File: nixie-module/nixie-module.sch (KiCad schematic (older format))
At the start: 4 parts, among them P1 CONN_02X05, U1 74141

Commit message: Kondensator przy zasilaniu ukladu 74141
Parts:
- added C1: 100n, symbol C
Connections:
- net GND: now also C1.2
- net VCC: now also C1.1
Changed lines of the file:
@@
 Connection ~ 2350 3450
 Connection ~ 2600 4050
+$Comp
+L C C1
+U 1 1 5832D96B
+P 2700 2800
+F 0 "C1" H 2725 2900 50  0000 L CNN
+F 1 "100n" H 2725 2700 50  0000 L CNN
+F 2 "" H 2738 2650 50  0000 C CNN
+F 3 "" H 2700 2800 50  0000 C CNN
+	1    2700 2800
+	1    0    0    -1
+$EndComp
+$Comp
+L GND #PWR?
+U 1 1 5832DA1C
+P 2700 3050
+F 0 "#PWR?" H 2700 2800 50  0001 C CNN
+F 1 "GND" H 2700 2900 50  0000 C CNN
+F 2 "" H 2700 3050 50  0000 C CNN
+F 3 "" H 2700 3050 50  0000 C CNN
+	1    2700 3050
+	1    0    0    -1
+$EndComp
+Wire Wire Line
+	2700 2650 2700 2550
+Wire Wire Line
+	2700 2550 2350 2550
+Connection ~ 2350 2550
+Wire Wire Line
+	2700 2950 2700 3050
 $EndSCHEMATC

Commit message: Przypisanie elementow (poza lampa) do obudow
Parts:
- C1: footprint (none) -> Capacitors_SMD:C_0805_HandSoldering
- P1: footprint (none) -> Pin_Headers:Pin_Header_Angled_2x05
- R1: footprint (none) -> Resistors_SMD:R_1812_HandSoldering
- U1: footprint (none) -> Housings_DIP:DIP-16_W7.62mm_LongPads
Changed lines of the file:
@@
 F 0 "U1" H 4950 3700 50  0000 C CNN
 F 1 "74141" H 5250 3100 50  0000 C CNN
-F 2 "" H 4950 3700 60  0001 C CNN
+F 2 "Housings_DIP:DIP-16_W7.62mm_LongPads" H 4950 3700 60  0001 C CNN
 F 3 "" H 4950 3700 60  0001 C CNN
 	1    4950 3700
@@
 F 0 "R1" V 7080 2950 50  0000 C CNN
 F 1 "100k" V 7000 2950 50  0000 C CNN
-F 2 "" V 6930 2950 50  0000 C CNN
+F 2 "Resistors_SMD:R_1812_HandSoldering" V 6930 2950 50  0001 C CNN
 F 3 "" H 7000 2950 50  0000 C CNN
 	1    7000 2950
@@
 F 0 "P1" H 2900 3950 50  0000 C CNN
 F 1 "CONN_02X05" H 2900 3350 50  0000 C CNN
-F 2 "" H 2900 2450 50  0000 C CNN
+F 2 "Pin_Headers:Pin_Header_Angled_2x05" H 2900 2450 50  0001 C CNN
 F 3 "" H 2900 2450 50  0000 C CNN
 	1    2900 3650
@@
 F 0 "C1" H 2725 2900 50  0000 L CNN
 F 1 "100n" H 2725 2700 50  0000 L CNN
-F 2 "" H 2738 2650 50  0000 C CNN
+F 2 "Capacitors_SMD:C_0805_HandSoldering" H 2738 2650 50  0001 C CNN
 F 3 "" H 2700 2800 50  0000 C CNN
 	1    2700 2800
@@
 $EndComp
 $Comp
-L GND #PWR?
+L GND #PWR06
 U 1 1 5832DA1C
 P 2700 3050
-F 0 "#PWR?" H 2700 2800 50  0001 C CNN
+F 0 "#PWR06" H 2700 2800 50  0001 C CNN
 F 1 "GND" H 2700 2900 50  0000 C CNN
 F 2 "" H 2700 3050 50  0000 C CNN

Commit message: Poprawienie pinow w gniezdzie
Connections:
- net A: now also P1.7 (P7); no longer P1.3 (P3)
- net B: now also P1.5 (P5); no longer P1.4 (P4)
- net C: now also P1.3 (P3); no longer P1.5 (P5)
- net D: now also P1.1 (P1); no longer P1.6 (P6)
- net GND: now also P1.4 (P4), P1.6 (P6); no longer P1.10 (P10), P1.7 (P7), P1.9 (P9)
- net VCC: now also P1.10 (P10); no longer P1.1 (P1)
- no-connect marks 0 -> 1
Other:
- moved on the sheet: C1
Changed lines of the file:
@@
 L VCC #PWR02
 U 1 1 5818D793
-P 2350 2450
-F 0 "#PWR02" H 2350 2300 50  0001 C CNN
-F 1 "VCC" H 2350 2600 50  0000 C CNN
-F 2 "" H 2350 2450 50  0000 C CNN
-F 3 "" H 2350 2450 50  0000 C CNN
-	1    2350 2450
+P 3550 3800
+F 0 "#PWR02" H 3550 3650 50  0001 C CNN
+F 1 "VCC" H 3550 3950 50  0000 C CNN
+F 2 "" H 3550 3800 50  0000 C CNN
+F 3 "" H 3550 3800 50  0000 C CNN
+	1    3550 3800
 	1    0    0    -1
 $EndComp
@@
 Wire Wire Line
 	3150 2650 3150 3450
-Wire Wire Line
-	2200 3450 2650 3450
-Wire Wire Line
-	2350 3450 2350 2450
 $Comp
 L GND #PWR03
@@
 $EndComp
 Wire Wire Line
-	3150 3750 3250 3750
+	3250 3750 3150 3750
 Wire Wire Line
-	3250 3750 3250 4300
-Wire Wire Line
-	3150 3850 3250 3850
-Connection ~ 3250 3850
-Wire Wire Line
-	2650 3750 2600 3750
-Wire Wire Line
-	2600 3750 2600 4050
-Wire Wire Line
-	2650 3850 2600 3850
-Connection ~ 2600 3850
+	3250 3550 3250 4300
 Wire Wire Line
 	2500 3550 2650 3550
@@
 	2500 3650 2650 3650
 Wire Wire Line
-	3350 3550 3150 3550
+	3250 3550 3150 3550
 Wire Wire Line
-	3150 3650 3350 3650
+	3150 3650 3250 3650
+Text Label 2500 3750 0    60   ~ 0
+A
+Text Label 2500 3650 0    60   ~ 0
+B
+Text Label 2500 3450 0    60   ~ 0
+D
 Text Label 2500 3550 0    60   ~ 0
-A
-Text Label 3350 3550 2    60   ~ 0
-B
-Text Label 3350 3650 2    60   ~ 0
-D
-Text Label 2500 3650 0    60   ~ 0
 C
 Wire Wire Line
@@
 D
 Wire Wire Line
-	2200 4050 3250 4050
-Connection ~ 3250 4050
+	3050 4200 3250 4200
+Connection ~ 3250 4200
 $Comp
 L PWR_FLAG #FLG04
 U 1 1 5818EF8B
-P 2200 4050
-F 0 "#FLG04" H 2200 4145 50  0001 C CNN
-F 1 "PWR_FLAG" H 2200 4230 50  0000 C CNN
-F 2 "" H 2200 4050 50  0000 C CNN
-F 3 "" H 2200 4050 50  0000 C CNN
-	1    2200 4050
+P 3050 4200
+F 0 "#FLG04" H 3050 4295 50  0001 C CNN
+F 1 "PWR_FLAG" H 3050 4380 50  0000 C CNN
+F 2 "" H 3050 4200 50  0000 C CNN
+F 3 "" H 3050 4200 50  0000 C CNN
+	1    3050 4200
 	0    -1   -1   0
 $EndComp
 $Comp
-L PWR_FLAG #FLG05
-U 1 1 5818EFE3
-P 2200 3450
-F 0 "#FLG05" H 2200 3545 50  0001 C CNN
-F 1 "PWR_FLAG" H 2200 3630 50  0000 C CNN
-F 2 "" H 2200 3450 50  0000 C CNN
-F 3 "" H 2200 3450 50  0000 C CNN
-	1    2200 3450
-	0    -1   -1   0
-$EndComp
-Connection ~ 2350 3450
-Connection ~ 2600 4050
-$Comp
 L C C1
 U 1 1 5832D96B
-P 2700 2800
-F 0 "C1" H 2725 2900 50  0000 L CNN
-F 1 "100n" H 2725 2700 50  0000 L CNN
-F 2 "Capacitors_SMD:C_0805_HandSoldering" H 2738 2650 50  0001 C CNN
-F 3 "" H 2700 2800 50  0000 C CNN
-	1    2700 2800
+P 3550 4100
+F 0 "C1" H 3575 4200 50  0000 L CNN
+F 1 "100n" H 3575 4000 50  0000 L CNN
+F 2 "Capacitors_SMD:C_0805_HandSoldering" H 3588 3950 50  0001 C CNN
+F 3 "" H 3550 4100 50  0000 C CNN
+	1    3550 4100
 	1    0    0    -1
 $EndComp
 $Comp
-L GND #PWR06
+L GND #PWR05
 U 1 1 5832DA1C
-P 2700 3050
-F 0 "#PWR06" H 2700 2800 50  0001 C CNN
-F 1 "GND" H 2700 2900 50  0000 C CNN
-F 2 "" H 2700 3050 50  0000 C CNN
-F 3 "" H 2700 3050 50  0000 C CNN
-	1    2700 3050
+P 3550 4300
+F 0 "#PWR05" H 3550 4050 50  0001 C CNN
+F 1 "GND" H 3550 4150 50  0000 C CNN
+F 2 "" H 3550 4300 50  0000 C CNN
+F 3 "" H 3550 4300 50  0000 C CNN
+	1    3550 4300
 	1    0    0    -1
 $EndComp
 Wire Wire Line
-	2700 2650 2700 2550
+	2500 3750 2650 3750
+Connection ~ 3250 3750
+Connection ~ 3250 3650
 Wire Wire Line
-	2700 2550 2350 2550
-Connection ~ 2350 2550
+	3150 3850 3750 3850
 Wire Wire Line
-	2700 2950 2700 3050
+	3550 3800 3550 3950
+Connection ~ 3550 3850
+Wire Wire Line
+	3550 4250 3550 4300
+$Comp
+L PWR_FLAG #FLG06
+U 1 1 5852B8CE
+P 3750 3850
+F 0 "#FLG06" H 3750 3945 50  0001 C CNN
+F 1 "PWR_FLAG" H 3750 4030 50  0000 C CNN
+F 2 "" H 3750 3850 50  0000 C CNN
+F 3 "" H 3750 3850 50  0000 C CNN
+	1    3750 3850
+	0    1    1    0
+$EndComp
+Wire Wire Line
+	2500 3450 2650 3450
+NoConn ~ 2650 3850
 $EndSCHEMATC

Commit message: Lokalna biblioteka footprint - nixie module; tymczasowe gniazdo do lampy
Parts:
- E1: footprint (none) -> nixie-module-footprint:b13b-valve-socket
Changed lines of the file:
@@
 F 0 "E1" H 6725 3475 60  0000 C CNN
 F 1 "GN-4P" H 6625 3900 60  0000 C CNN
-F 2 "" H 6250 3700 60  0001 C CNN
+F 2 "nixie-module-footprint:b13b-valve-socket" H 6250 3700 60  0001 C CNN
 F 3 "" H 6250 3700 60  0001 C CNN
 	1    6200 3700

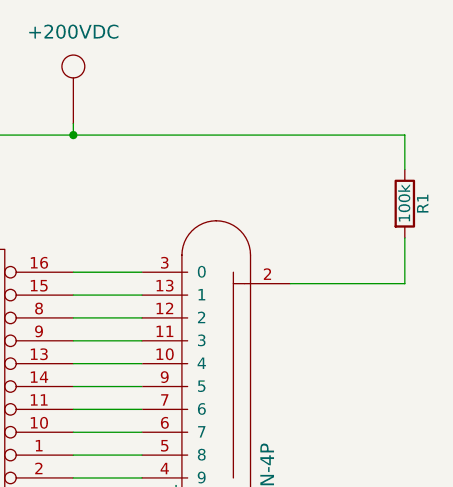
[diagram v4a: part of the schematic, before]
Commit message: Gotowe gniazdo na GN4P - wlutowanie nitow 1mm
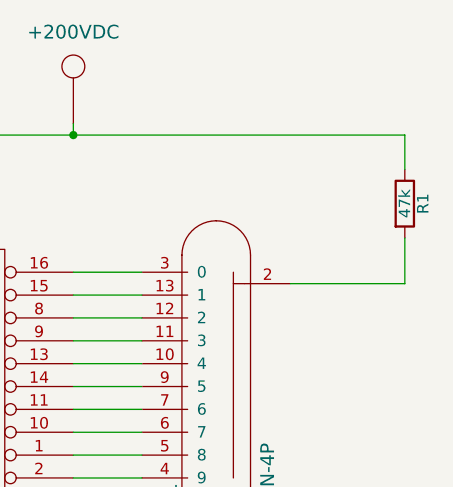
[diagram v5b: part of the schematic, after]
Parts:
- E1: footprint nixie-module-footprint:b13b-valve-socket -> nixie-module-footprint:gn-4p-gniazdo
- R1: value 100k -> 47k
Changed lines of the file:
@@
 F 0 "E1" H 6725 3475 60  0000 C CNN
 F 1 "GN-4P" H 6625 3900 60  0000 C CNN
-F 2 "nixie-module-footprint:b13b-valve-socket" H 6250 3700 60  0001 C CNN
+F 2 "nixie-module-footprint:gn-4p-gniazdo" H 6250 3700 60  0001 C CNN
 F 3 "" H 6250 3700 60  0001 C CNN
 	1    6200 3700
@@
 P 7000 2950
 F 0 "R1" V 7080 2950 50  0000 C CNN
-F 1 "100k" V 7000 2950 50  0000 C CNN
+F 1 "47k" V 7000 2950 50  0000 C CNN
 F 2 "Resistors_SMD:R_1812_HandSoldering" V 6930 2950 50  0001 C CNN
 F 3 "" H 7000 2950 50  0000 C CNN

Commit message: Odwrocenie numeracji pinow w zlaczu od modulu NIXIE
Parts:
- P1: footprint Pin_Headers:Pin_Header_Angled_2x05 -> nixie-module-footprint:Pin_Header_Angled_2x05
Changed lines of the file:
@@
 F 0 "P1" H 2900 3950 50  0000 C CNN
 F 1 "CONN_02X05" H 2900 3350 50  0000 C CNN
-F 2 "Pin_Headers:Pin_Header_Angled_2x05" H 2900 2450 50  0001 C CNN
+F 2 "nixie-module-footprint:Pin_Header_Angled_2x05" H 2900 2450 50  0001 C CNN
 F 3 "" H 2900 2450 50  0000 C CNN
 	1    2900 3650
